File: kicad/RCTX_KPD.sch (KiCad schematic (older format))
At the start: 27 parts, among them P39 KEYBOARD

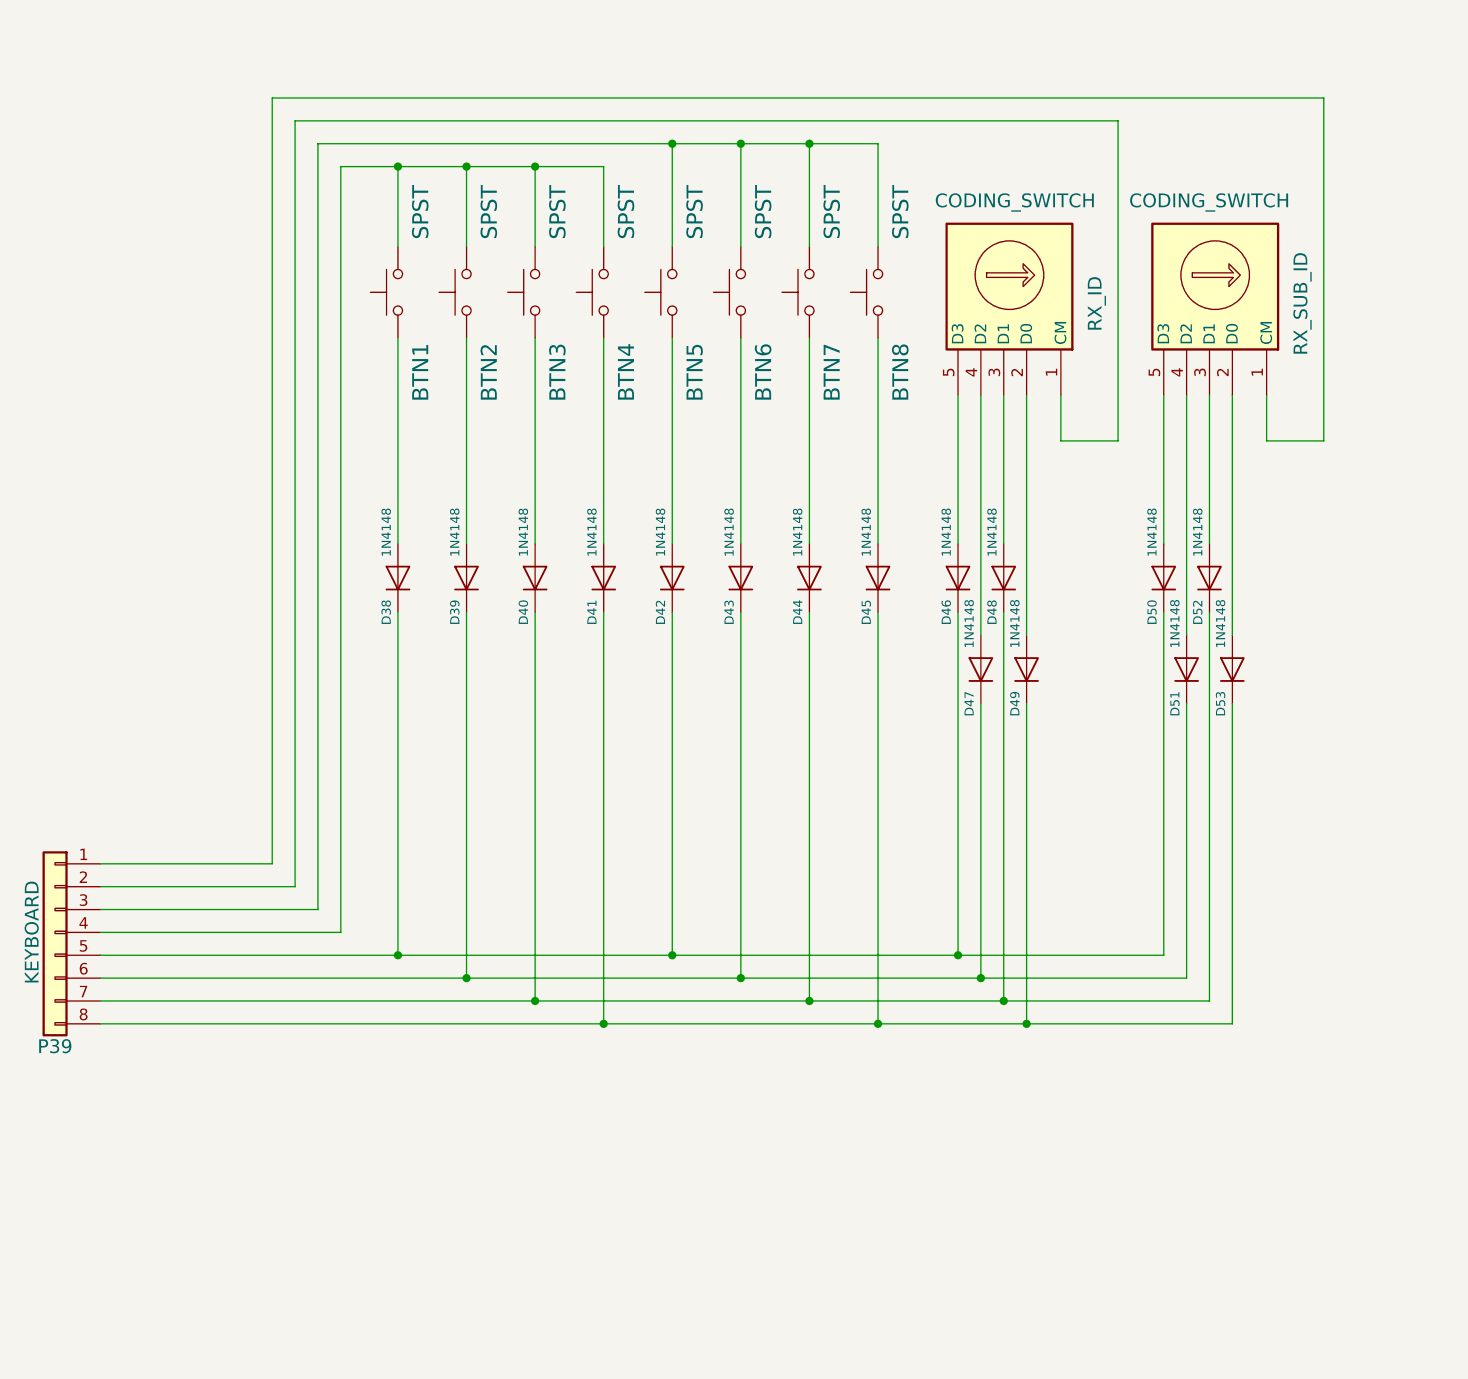
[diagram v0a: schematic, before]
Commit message: New rx-tx bidirectional amplifier
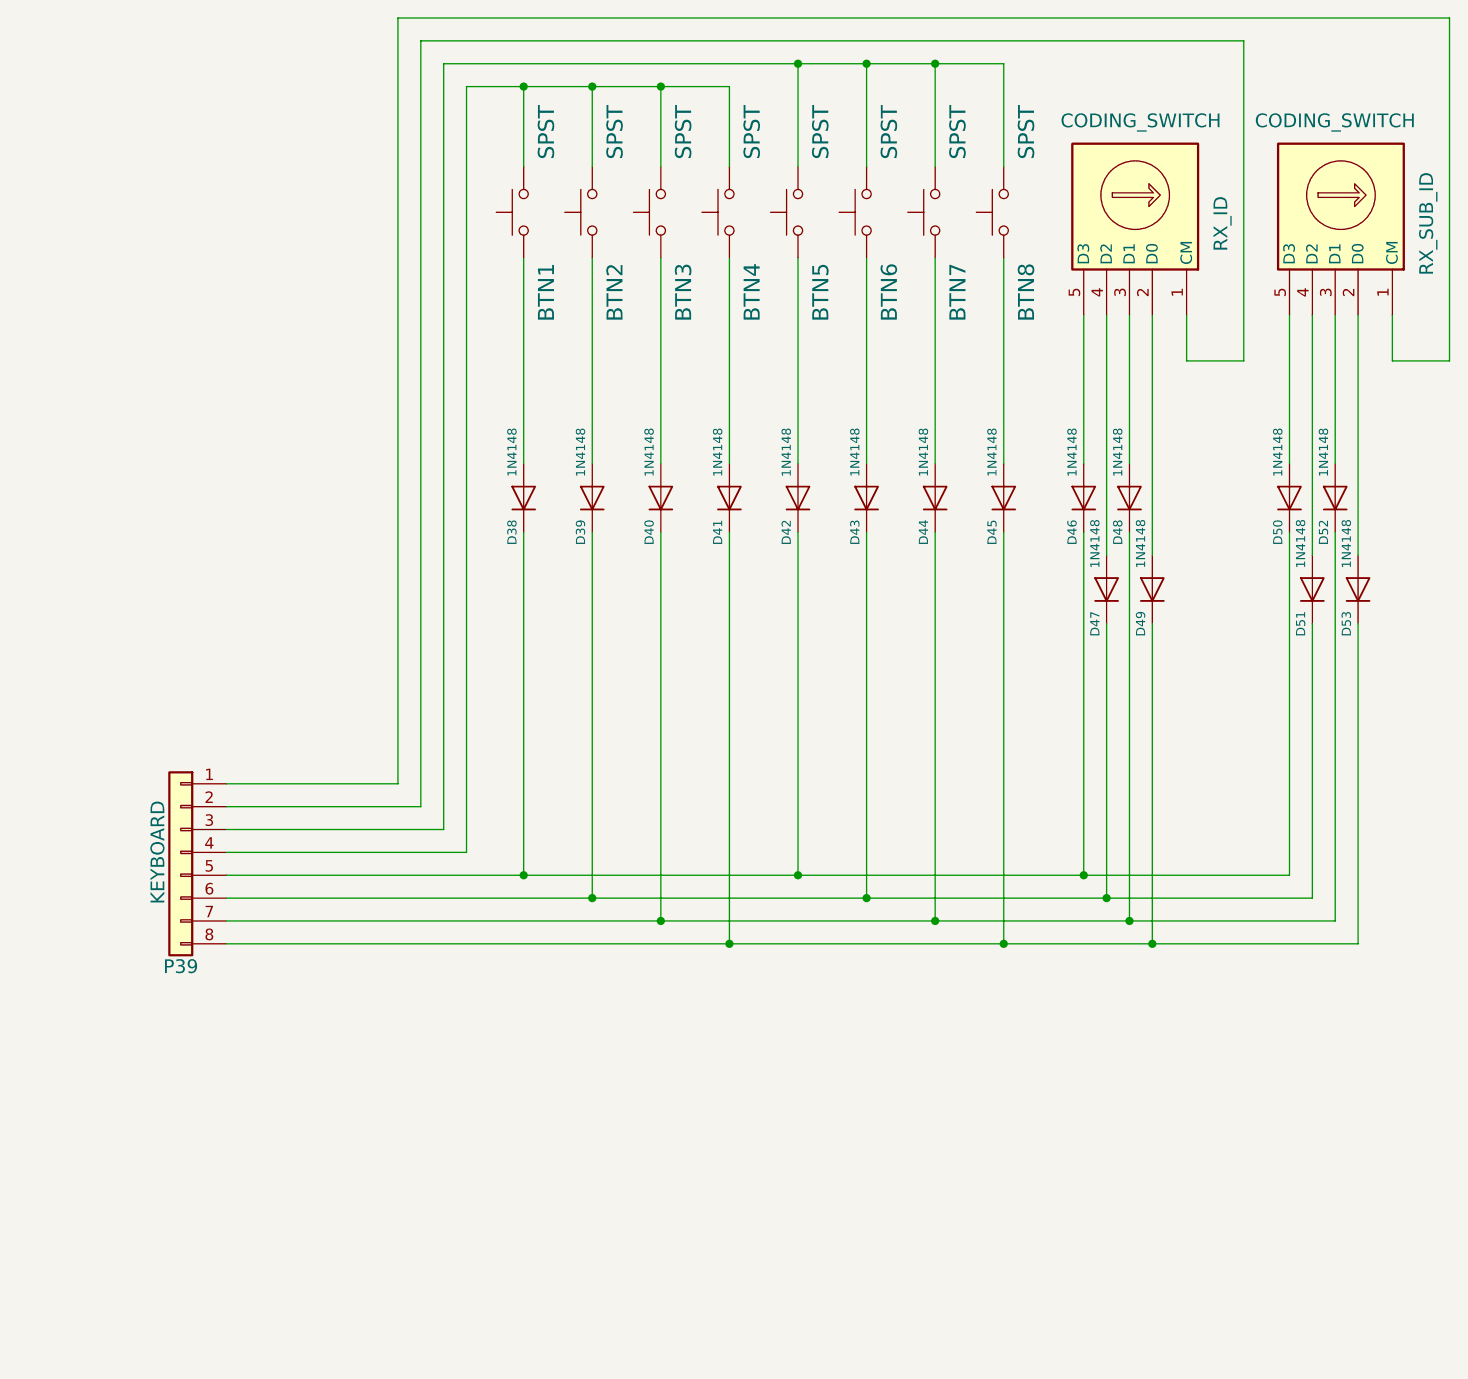
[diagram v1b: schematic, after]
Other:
- moved on the sheet: BTN1, BTN2, BTN3, BTN4, BTN5, BTN6, BTN7, BTN8, D38, D39, D40, D41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

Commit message: Using ERF32FG12 SoC instead of PIC32MX
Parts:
- added P?: SW, Connectors_Samtec:SL-103-X-XX_1x03, symbol RCTX-rescue:Conn_01x03-conn
- added P?: PWR_BUS, Connectors_Samtec:SL-104-X-XX_1x04, symbol RCTX-rescue:Conn_01x04-conn
- added SW?: Reset, Buttons_Switches_THT:SW_PUSH_6mm_h5mm, symbol RCTX-rescue:SW_SPST-switches
- added SW?: Program, Buttons_Switches_THT:SW_PUSH_6mm_h5mm, symbol RCTX-rescue:SW_SPST-switches
- added SW?: User, Buttons_Switches_THT:SW_PUSH_6mm_h5mm, symbol RCTX-rescue:SW_SPST-switches
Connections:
- new net: P?.1 (Pin_1), SW?.2 (B)
- new net: P?.2 (Pin_2), SW?.2 (B)
- new net: P?.3 (Pin_3), SW?.2 (B)
- new net GND: P?.3 (Pin_3), SW?.1 (A), SW?.1 (A), SW?.1 (A)
- no-connect marks 0 -> 3
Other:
- note added: "+3.3V"
- note added: "+5V"
- note added: "GND"
- note added: "Program"
- note added: "Reset"
- note added: "User"
- note added: "VBAT+"
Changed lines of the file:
@@
 $Descr A4 11693 8268
 encoding utf-8
-Sheet 10 11
+Sheet 10 13
 Title "Buttons and encoders"
 Date "2020-04-15"
@@
 	0    -1   -1   0
 $EndComp
+Wire Wire Line
+	3550 7100 3550 6750
+Wire Wire Line
+	3550 6750 3550 6400
+$Comp
+L RCTX-rescue:SW_SPST-switches SW?
+U 1 1 6017CE9A
+P 4150 6400
+F 0 "SW?" H 4150 6500 70  0000 C CNN
+F 1 "Reset" H 3300 6400 70  0000 C CNN
+F 2 "Buttons_Switches_THT:SW_PUSH_6mm_h5mm" H 4150 6400 50  0001 C CNN
+F 3 "" H 4150 6400 50  0001 C CNN
+	1    4150 6400
+	1    0    0    -1
+$EndComp
+$Comp
+L RCTX-rescue:SW_SPST-switches SW?
+U 1 1 6017CEA0
+P 4150 6750
+F 0 "SW?" H 4150 6850 70  0000 C CNN
+F 1 "Program" H 3250 6750 70  0000 C CNN
+F 2 "Buttons_Switches_THT:SW_PUSH_6mm_h5mm" H 4150 6750 50  0001 C CNN
+F 3 "" H 4150 6750 50  0001 C CNN
+	1    4150 6750
+	1    0    0    -1
+$EndComp
+$Comp
+L RCTX-rescue:SW_SPST-switches SW?
+U 1 1 6017CEA6
+P 4150 7100
+F 0 "SW?" H 4150 7200 70  0000 C CNN
+F 1 "User" H 3350 7100 70  0000 C CNN
+F 2 "Buttons_Switches_THT:SW_PUSH_6mm_h5mm" H 4150 7100 50  0001 C CNN
+F 3 "" H 4150 7100 50  0001 C CNN
+	1    4150 7100
+	1    0    0    -1
+$EndComp
+$Comp
+L RCTX-rescue:Conn_01x03-conn P?
+U 1 1 6017CEAC
+P 5400 6500
+F 0 "P?" H 5400 6300 50  0000 C CNN
+F 1 "SW" V 5500 6500 40  0000 C CNN
+F 2 "Connectors_Samtec:SL-103-X-XX_1x03" H 5400 6500 50  0001 C CNN
+F 3 "" H 5400 6500 50  0001 C CNN
+	1    5400 6500
+	1    0    0    -1
+$EndComp
+NoConn ~ 5200 7100
+NoConn ~ 5200 7200
+NoConn ~ 5200 7400
+Text Notes 5700 6450 0    60   ~ 0
+Reset
+Text Notes 5700 6550 0    60   ~ 0
+Program
+Text Notes 5700 6650 0    60   ~ 0
+User
+Connection ~ 3550 7100
+Wire Wire Line
+	3550 7100 3950 7100
+Wire Wire Line
+	3550 6400 3950 6400
+Wire Wire Line
+	3550 7300 3550 7100
+Wire Wire Line
+	5200 7300 3550 7300
+Wire Wire Line
+	4750 6500 5200 6500
+Wire Wire Line
+	4750 6750 4750 6500
+Wire Wire Line
+	4350 6750 4750 6750
+Wire Wire Line
+	5200 6400 4350 6400
+Wire Wire Line
+	4850 7100 4350 7100
+Wire Wire Line
+	4850 6600 4850 7100
+Wire Wire Line
+	5200 6600 4850 6600
+Wire Wire Line
+	3550 6750 3950 6750
+Connection ~ 3550 6750
+Text Notes 5950 7150 2    60   ~ 0
++3.3V
+Text Notes 5700 7350 0    60   ~ 0
+GND
+Text Notes 5700 7250 0    60   ~ 0
++5V
+Text Notes 5700 7450 0    60   ~ 0
+VBAT+
+$Comp
+L RCTX-rescue:Conn_01x04-conn P?
+U 1 1 6017CECA
+P 5400 7200
+F 0 "P?" H 5350 6900 50  0000 L CNN
+F 1 "PWR_BUS" V 5500 7000 50  0000 L CNN
+F 2 "Connectors_Samtec:SL-104-X-XX_1x04" H 5400 7200 50  0001 C CNN
+F 3 "~" H 5400 7200 50  0001 C CNN
+	1    5400 7200
+	1    0    0    -1
+$EndComp
+$Comp
+L RCTX-rescue:GND-power #PWR?
+U 1 1 6017CED0
+P 3550 7400
+F 0 "#PWR?" H 3550 7150 50  0001 C CNN
+F 1 "GND" H 3555 7227 50  0000 C CNN
+F 2 "" H 3550 7400 50  0001 C CNN
+F 3 "" H 3550 7400 50  0001 C CNN
+	1    3550 7400
+	1    0    0    -1
+$EndComp
+Wire Wire Line
+	3550 7300 3550 7400
+Connection ~ 3550 7300
 $EndSCHEMATC
